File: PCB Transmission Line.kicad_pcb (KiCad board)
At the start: 2 copper layers, 200 x 100 mm, 7 parts, among them J1 KH-BNC50-3511, J2 KH-BNC50-3511, J3 KH-BNC50-3511

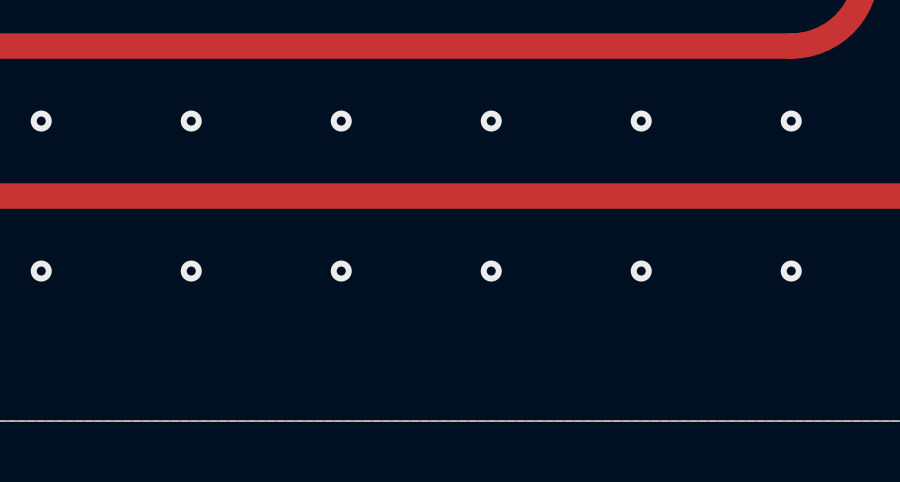
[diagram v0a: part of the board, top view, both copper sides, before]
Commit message: Add silkscreen notes and equations
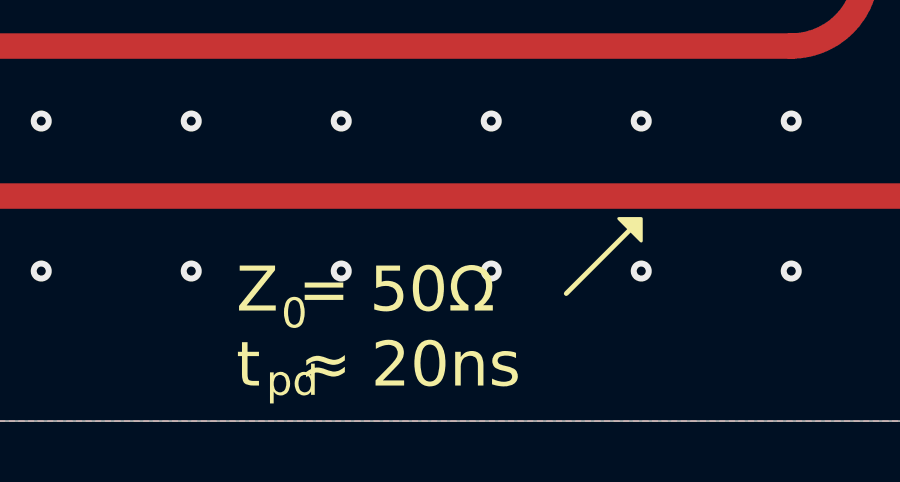
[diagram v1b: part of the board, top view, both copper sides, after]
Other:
- board text added: "(*)Used in this board."
- board text added: "0"
- board text added: "Characteristic Impedance:"
- board text added: "Coplanar Waveguide with Ground Plane (*)"
- board text added: "Copper"
- board text added: "Dielectric"
- board text added: "Embedded Microstrip"
- board text added: "L"
- board text added: "Legend"
- board text added: "Microstrip"
- board text added: "PCB Transmission Line v1.0 © Leonardo Márquez, 2025 @marqueztronics https://github.com/marqueztronics/PCB-Transmission-Line"
- board text added: "Propagation Speed:"
- board text added: "R"
- board text added: "Reflection Coefficient:"
- board text added: "Stackup Table"
- board text added: "Stripline"
- board text added: "Transmission Line Geometries"
- board text added: "Useful Equations"
- board text added: "Where: L: Inductance per unit-length C: Capacitance per unit-length Z : Load impedance c: Speed of light in vacuum ε : Relative permittivity μ : Relative permeability"
- board text added: "Z = 50Ω"
- board text added: "pd"
- board text added: "t ≈ 20ns"
- board text removed: "PCB Transmission Line v1.0 (c) 2025, Leonardo Márquez @marqueztronics"

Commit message: Finish silkscreen notes and plot Gerber files
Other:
- board text added: "PCB Transmission Line"
- board text added: "© Leonardo Márquez, 2025 @marqueztronics https://github.com/marqueztronics/PCB-Transmission-Line"
- board text removed: "PCB Transmission Line v1.0 © Leonardo Márquez, 2025 @marqueztronics https://github.com/marqueztronics/PCB-Transmission-Line"
